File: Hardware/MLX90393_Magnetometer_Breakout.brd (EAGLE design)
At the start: 25.4 x 23.5 mm, 15 parts, among them U1 MLX90393_MAGNETOMETER

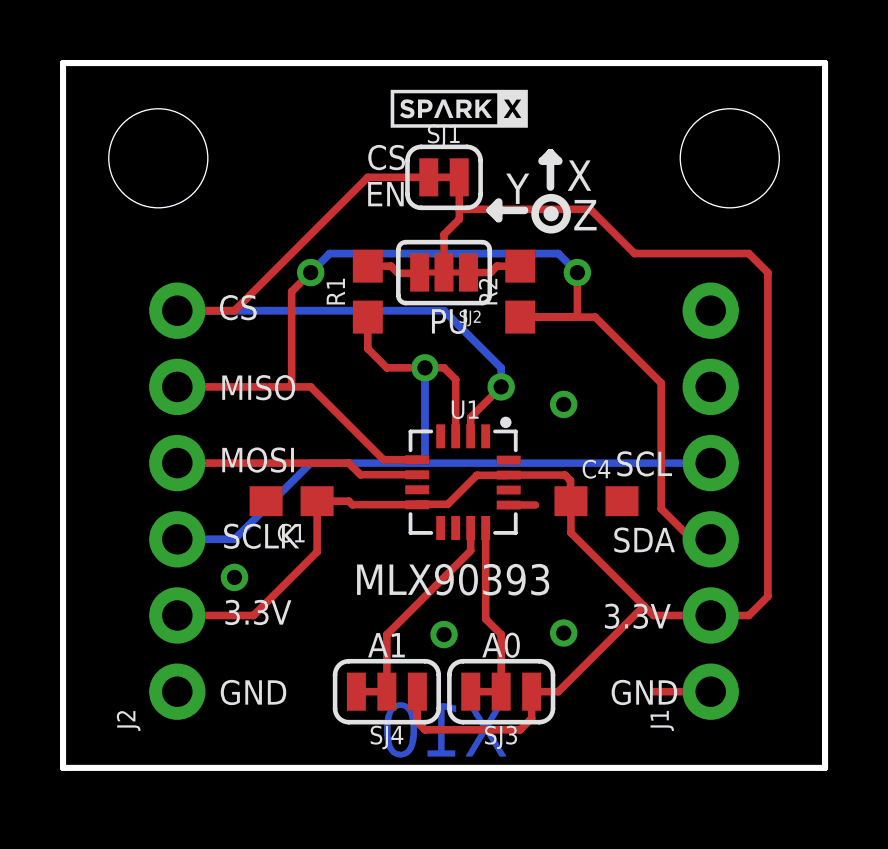
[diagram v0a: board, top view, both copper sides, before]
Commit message: Bringing back production layout: missing top mask on QFN.
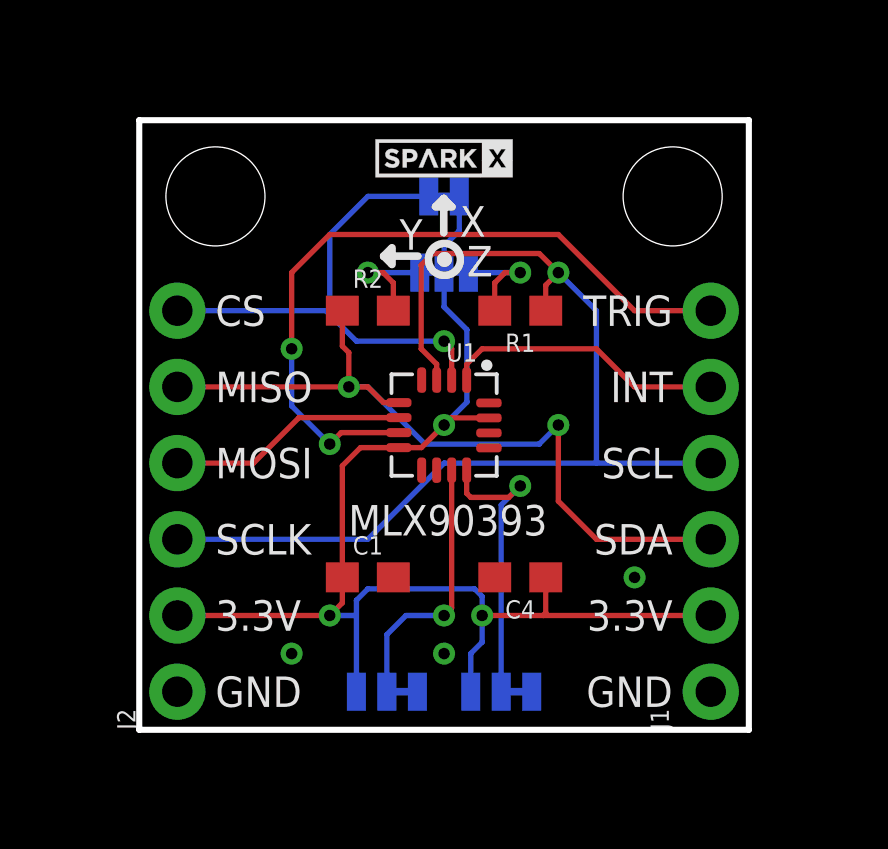
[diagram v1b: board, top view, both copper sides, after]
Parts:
- added U$1: OSHW-LOGOS, SparkFun:OSHW-LOGO-S
- moved R1 5.12 mm to (12.7, 14.0), turned to 180 degrees
- moved R2 5.12 mm to (7.62, 14.0), turned to 0 degrees
- moved C4 3.59 mm to (12.7, 5.08), turned to 180 degrees
- moved C1 3.59 mm to (7.62, 5.08), turned to 0 degrees
- moved JP3 2.29 mm to (2.54, 17.8)
- moved JP4 2.29 mm to (17.8, 17.8)
- moved U1 2.01 mm to (10.2, 10.2)
- moved U$2 1.73 mm to (10.2, 19.1)
- moved SJ1 0.63 mm to (10.2, 17.8), flipped to the bottom, turned to 180 degrees
- flipped SJ2 to the bottom
- flipped SJ3 to the bottom
- flipped SJ4 to the bottom
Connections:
- net VDD renamed 3.3V
- net INT: now also J1.5
- net TRIG: now also J1.6
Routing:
- net TRIG: track 0.00 -> 24.2 mm, vias 0 -> 2
- net 3.3V: track 62.2 -> 44.9 mm, vias 0 -> 3
- net SDA: track 37.8 -> 26.4 mm
- net INT: track 0.00 -> 9.40 mm
- net SCL: track 28.3 -> 36.2 mm
- net CS: track 24.5 -> 17.2 mm
- net A0: track 5.67 -> 9.89 mm, vias 0 -> 1
- net GND: track 2.79 -> 0.00 mm, vias 4 -> 3
- net A1: track 6.61 -> 9.02 mm, vias 0 -> 1
- net N$4: track 1.82 -> 3.65 mm, vias 0 -> 1
- net N$5: track 1.84 -> 3.65 mm, vias 0 -> 1
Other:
- board size 25.4 x 23.5 mm -> 20.3 x 20.3 mm
- board text added: "INT"
- board text added: "J. Bartlett"
- board text added: "TRIG"
- board text removed: "CS EN"
- board text removed: "X10"
